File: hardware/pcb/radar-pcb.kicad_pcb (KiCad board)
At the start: 2 copper layers, 66 x 128 mm, 71 parts, among them J1 USB-C zasilanie 5 V (GCT USB4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, J10 Awaryjne wgrywanie: BOOT GND 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, J2 DevKit J1, J3 DevKit J3, J4 HC-SR04 (kabel): VCC TRIG ECH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, J5 Serwo SG90 (kabel): GND +5V S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, J6 MAX7219 Elegoo: VCC GND DIN C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, J7 OLED SH1106: VCC GND SCK SDA, J8 Buzzer: + -, J9 Przycisk zewnetrzny, Q2 MMBT3904, SW1 Przycisk ON/standby (katowy), U1 SN74AHCT125D, U2 AP22804AW5 (przelacznik 5 V, 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

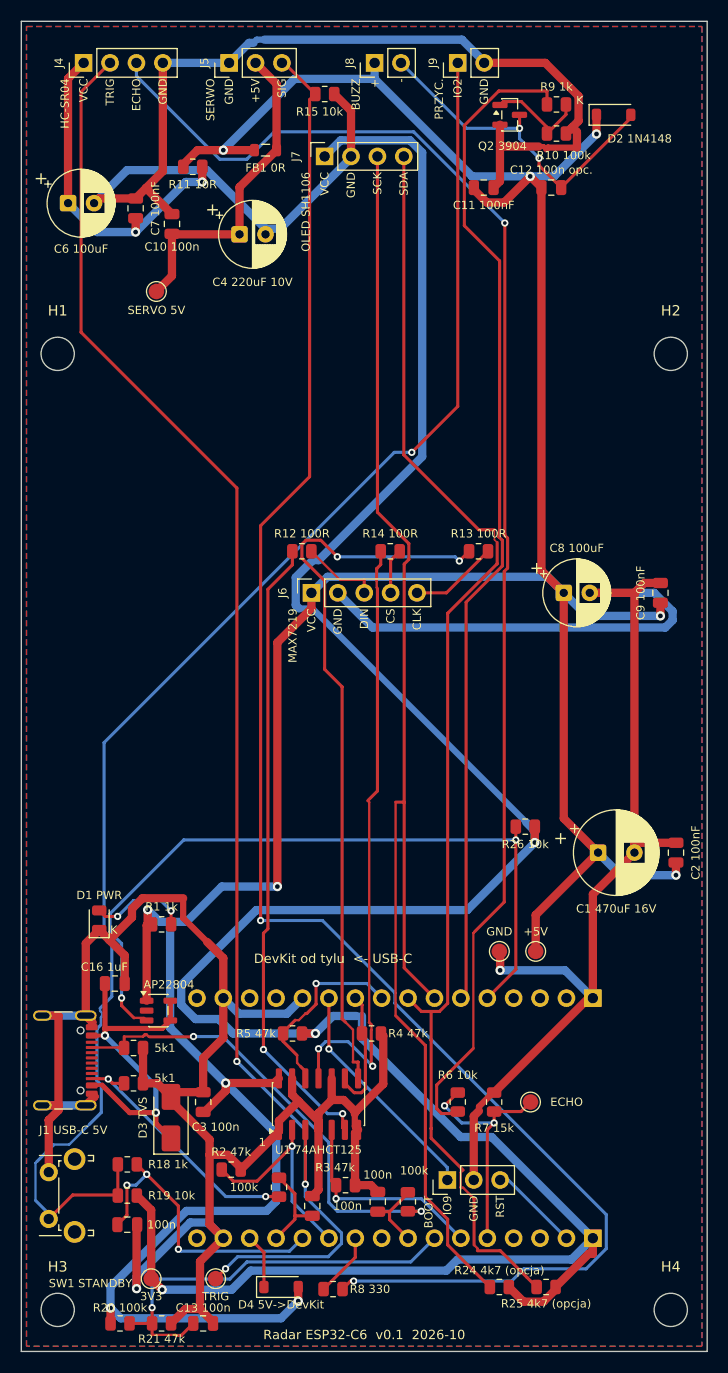
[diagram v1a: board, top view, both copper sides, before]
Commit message: PCB (wariant kompaktowy): moduły OLED i MAX7219 na kablach, płytka 66x101 mm zamiast 66x128 mm
Gniazda J7 i J6 zostają jako złącza kabli, środkowy pas płytki usunięty,
dolna grupa (zasilanie, DevKit, bufor) przesunięta o 27 mm w górę (DY w gen_pcb.py).
DRC: 0 naruszeń, 0 niepołączonych, 0 niezgodności ze schematem. Wymiary W3-W9
zmieniły położenie i są oznaczone ? do ponownego zatwierdzenia. Nie sprawdzone na sprzęcie.

Co-Authored-By: Claude Sonnet 5.5 <noreply@anthropic.com>
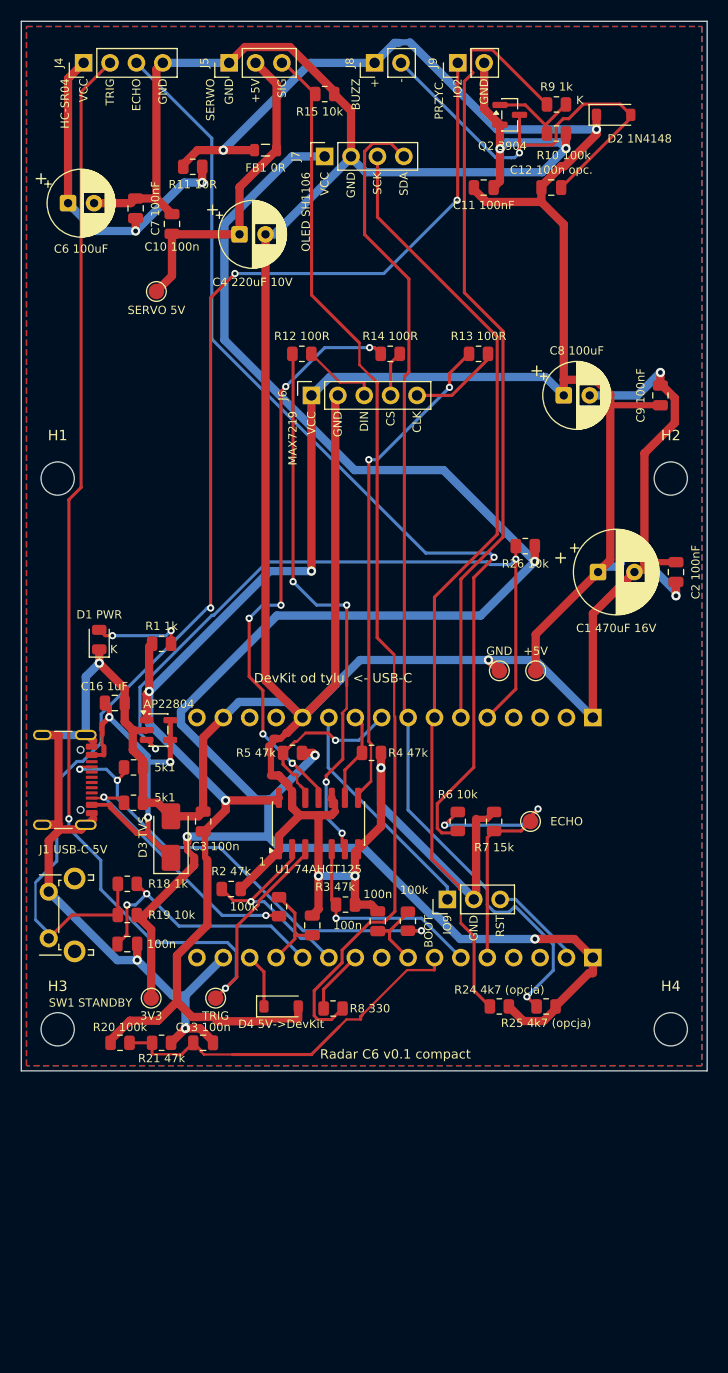
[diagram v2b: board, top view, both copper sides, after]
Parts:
- moved C13 27.0 mm to (117.5, 123.3)
- moved C5 27.0 mm to (110.2, 113.8)
- moved D4 27.0 mm to (125.0, 119.8)
- moved R20 27.0 mm to (109.5, 123.3)
- moved R21 27.0 mm to (113.5, 123.3)
- moved R24 27.0 mm to (146.0, 119.8)
- moved R25 27.0 mm to (150.5, 119.8)
- moved C1 27.0 mm to (155.5, 78.0)
- moved C14 27.0 mm to (134.3, 111.6)
- moved C15 27.0 mm to (128.0, 112.0)
- moved C16 27.0 mm to (109.0, 90.6)
- moved C2 27.0 mm to (163.0, 78.0)
- moved C3 27.0 mm to (117.5, 102.0)
- moved D1 27.0 mm to (107.5, 84.5)
- moved D3 27.0 mm to (114.4, 103.5)
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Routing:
- net SERVO_SIG: track 162.0 -> 103.9 mm, vias 2 -> 0
- net +5V: track 325.7 -> 272.8 mm, vias 10 -> 6
- net +3V3: track 254.3 -> 202.5 mm, vias 3 -> 4
- net SCL: track 134.9 -> 91.5 mm
- net ECHO_5V: track 135.3 -> 96.0 mm
- net SDA: track 125.0 -> 98.1 mm, vias 0 -> 1
- net TRIG_5V: track 143.9 -> 119.9 mm, vias 3 -> 2
- net CLK_5V: track 71.4 -> 47.8 mm
- net BTN: track 142.3 -> 121.1 mm, vias 1 -> 3
- net BUZ_CTRL: track 97.8 -> 77.4 mm
- net GND: track 446.6 -> 463.3 mm, vias 2 -> 10
- net BUZ_NEG: track 32.4 -> 42.4 mm, vias 2 -> 1
- net DIN_5V: track 60.9 -> 53.2 mm, vias 2 -> 4
- net ECHO_3V3: track 23.6 -> 29.3 mm
- net U2_FLG: track 71.9 -> 66.9 mm
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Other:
- board size 66 x 128 mm -> 66 x 101 mm
- board text added: "Radar C6 v0.1 compact"
- board text added: "W2 wysokosc plytki (wariant kompaktowy, moduly na kablach)"
- board text added: "W3 gniazdo kabla OLED (J7): od lewej krawedzi do pinu 1"
- board text added: "W4 gniazdo kabla MAX7219 (J6): od lewej krawedzi do pinu 1"
- board text removed: "Radar ESP32-C6 v0.1 2026-10"
- board text removed: "W2 wysokosc plytki: czy miesci sie w kolumnie nad podstawka"
- board text removed: "W3 OLED: od lewej krawedzi do pinu 1 gniazda J7 (okno ekranu w obudowie)"
- board text removed: "W4 MAX7219: od lewej krawedzi do pinu 1 gniazda J6 (okno matrycy)"
- board text removed: "W5 odstep gniazd OLED-MAX7219 (pion), ZMIERZONE 42,0 mm"

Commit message: PCB (wariant kompaktowy): skrócenie do 66x91 mm, C8/C9 i otwory M3 przestawione
DY = -37 mm, C8/C9 obok J6, górne otwory M3 w y = 30 mm. DRC: 0 naruszeń,
0 niepołączonych, 0 niezgodności ze schematem. Nie sprawdzone na sprzęcie.

Co-Authored-By: Claude Sonnet 5.5 <noreply@anthropic.com>
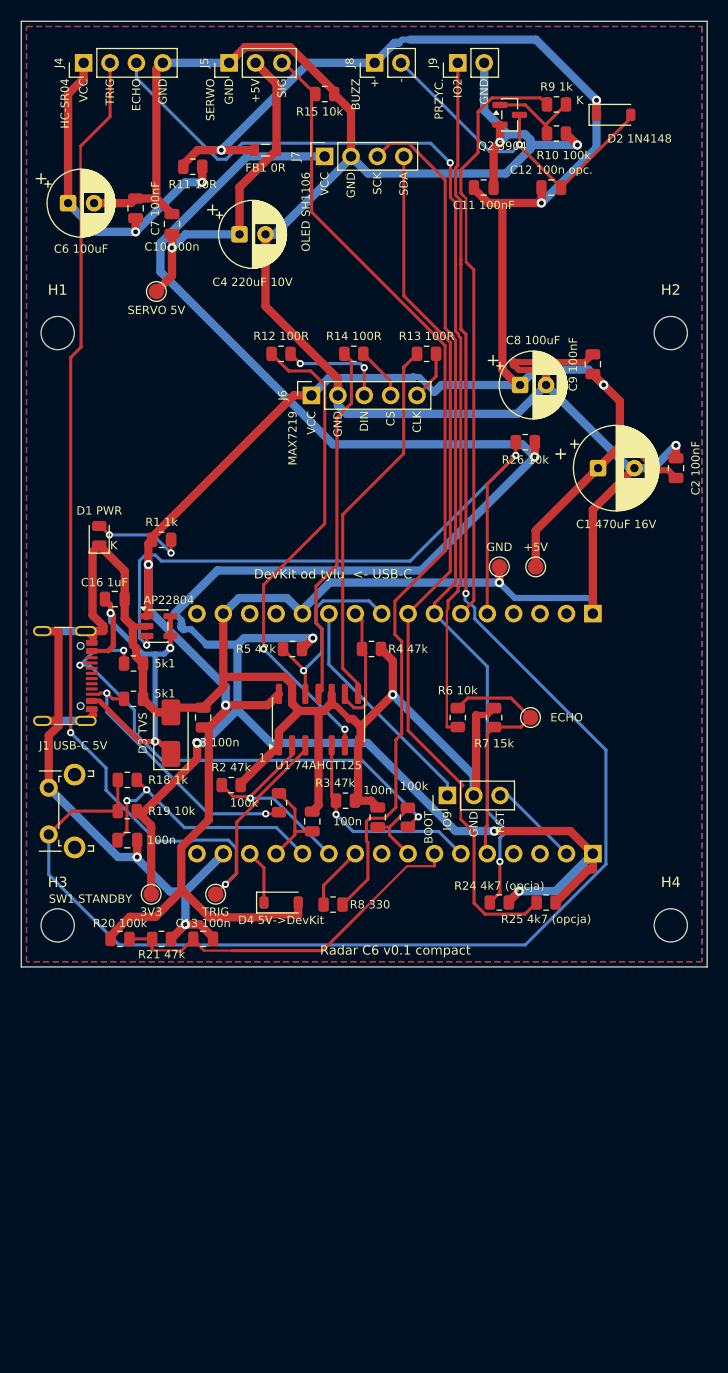
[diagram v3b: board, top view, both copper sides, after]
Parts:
- moved H1 14.0 mm to (103.5, 55.0)
- moved H2 14.0 mm to (162.5, 55.0)
- moved C1 10.0 mm to (155.5, 68.0)
- moved C13 10.0 mm to (117.5, 113.3)
- moved C14 10.0 mm to (134.3, 101.6)
- moved C15 10.0 mm to (128.0, 102.0)
- moved C16 10.0 mm to (109.0, 80.6)
- moved C2 10.0 mm to (163.0, 68.0)
- moved C3 10.0 mm to (117.5, 92.0)
- moved C5 10.0 mm to (110.2, 103.8)
- moved D1 10.0 mm to (107.5, 74.5)
- moved D3 10.0 mm to (114.4, 93.5)
- moved D4 10.0 mm to (125.0, 109.8)
- moved H3 10.0 mm to (103.5, 112.0)
- moved H4 10.0 mm to (162.5, 112.0)
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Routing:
- net GND: track 463.3 -> 418.2 mm, vias 10 -> 7
- net BTN: track 121.1 -> 157.4 mm, vias 3 -> 1
- net +5V: track 272.8 -> 245.5 mm
- net CS_5V: track 55.8 -> 34.8 mm, vias 6 -> 0
- net BUZ_CTRL: track 77.4 -> 57.5 mm
- net SDA: track 98.1 -> 85.1 mm, vias 1 -> 0
- net CLK_5V: track 47.8 -> 36.3 mm, vias 2 -> 0
- net SERVO_SIG: track 103.9 -> 93.5 mm
- net TRIG_5V: track 119.9 -> 109.8 mm
- net SCL: track 91.5 -> 82.6 mm, vias 0 -> 1
- net BUZ_NEG: track 42.4 -> 33.6 mm
- net +3V3: track 202.5 -> 210.1 mm, vias 4 -> 5
- net DIN_5V: track 53.2 -> 46.8 mm, vias 4 -> 2
- net ECHO_3V3: track 29.3 -> 24.7 mm, vias 2 -> 0
- net CC1: track 44.4 -> 48.6 mm
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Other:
- board size 66 x 101 mm -> 66 x 91 mm

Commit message: PCB: napisy 1 mm (wymóg JLCPCB), U2 zmieniony na AP22802AW5-7 (C211404)
Wszystkie napisy na silkscreenie mają wysokość 1,0 mm i grubość 0,17 mm, obrysy
elementów min. 0,15 mm; opisy przeorganizowane (C14/C15/R22/R23/R24/R25 w legendzie,
ukryte oznaczenia otworów). Dodany tryb relabel w gen_pcb.py. U2 pin w pin zamiennik,
bo AP22804AW5 nie ma w katalogu JLCPCB. ERC 0 błędów, DRC 0 naruszeń, 0 niepołączonych,
0 niezgodności ze schematem. Nie sprawdzone na sprzęcie.

Co-Authored-By: Claude Sonnet 5.5 <noreply@anthropic.com>
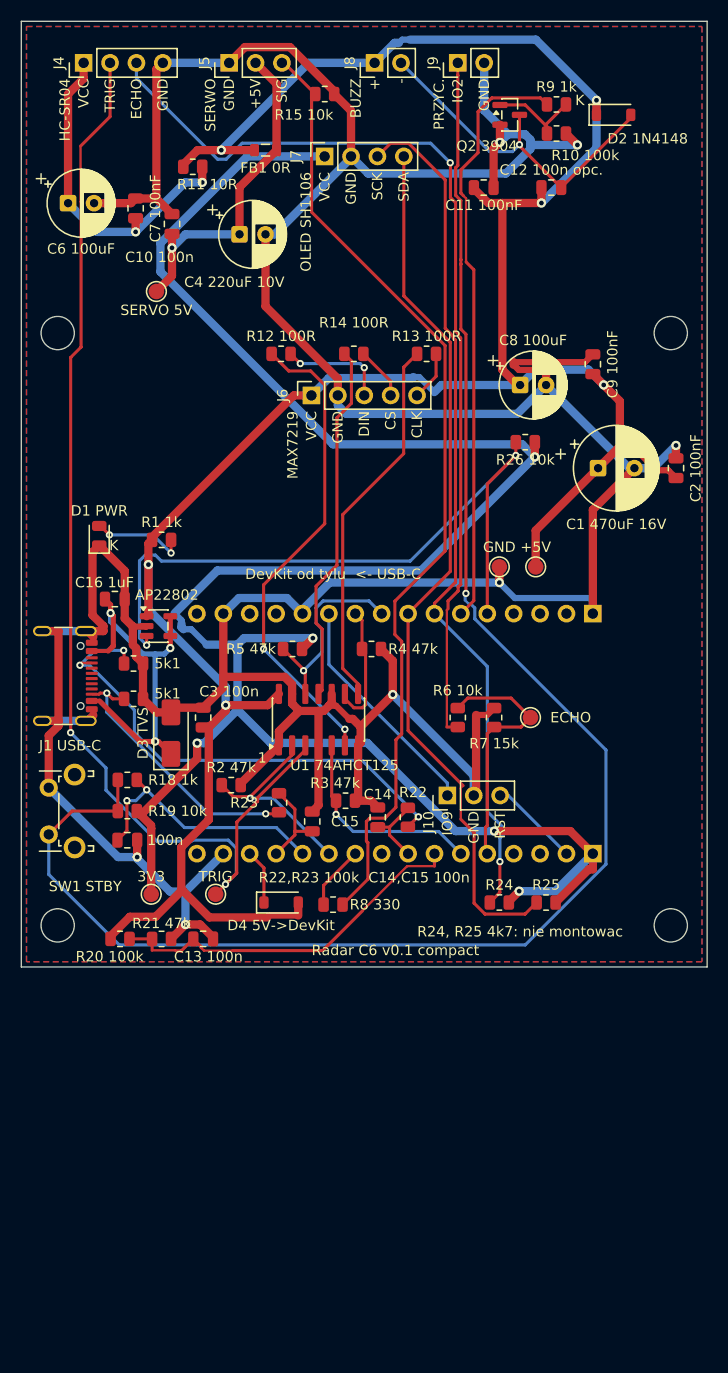
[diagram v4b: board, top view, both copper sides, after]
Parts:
- U2: value AP22804AW5 (przelacznik 5 V, limit ok. 2,5-3 A) -> AP22802AW5-7 (przelacznik 5 V, LCSC C211404, limit ok. 2,2-3,2 A)
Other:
- board text added: "AP22802"
- board text added: "C14"
- board text added: "C15"
- board text added: "J1 USB-C"
- board text added: "J10"
- board text added: "R22"
- board text added: "R22,R23 100k C14,C15 100n"
- board text added: "R23"
- board text added: "R24"
- board text added: "R24, R25 4k7: nie montowac"
- board text added: "R25"
- board text added: "SW1 STBY"
- board text removed: "100k"
- board text removed: "AP22804"
- board text removed: "BOOT"
- board text removed: "J1 USB-C 5V"
- board text removed: "R24 4k7 (opcja)"
- board text removed: "R25 4k7 (opcja)"
- board text removed: "SW1 STANDBY"
